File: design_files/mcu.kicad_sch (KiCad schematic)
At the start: 19 parts, among them J3 Conn_01x05, U1 STM32U545CEUx, U2 GD25QxxxEY, Y1 32.768KHz, Y2 8MHz

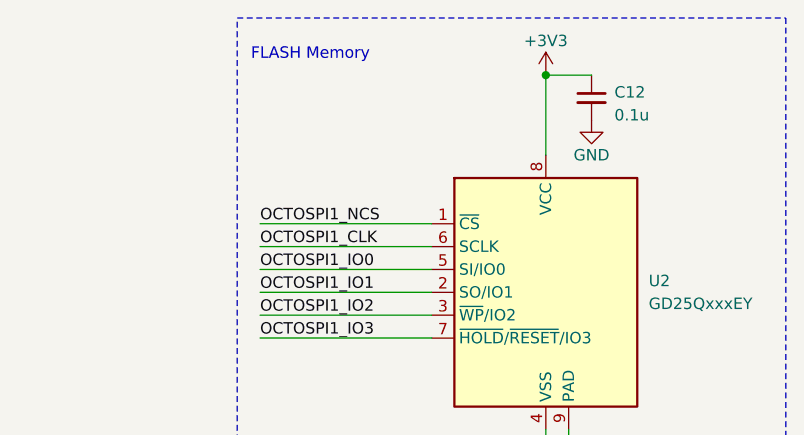
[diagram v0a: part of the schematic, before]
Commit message: Added CS pullup
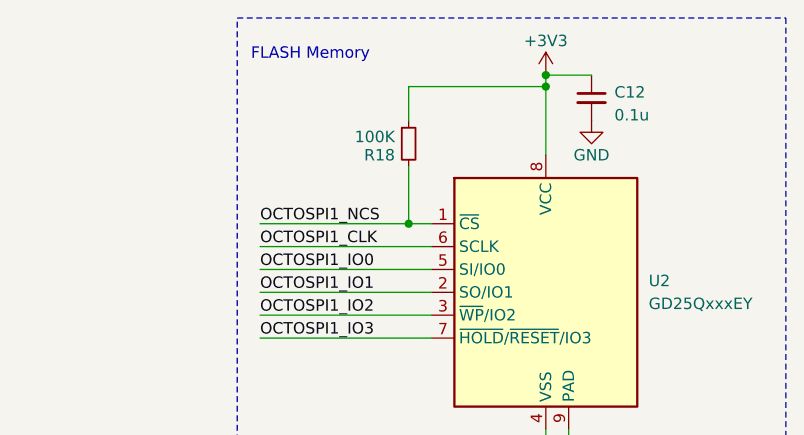
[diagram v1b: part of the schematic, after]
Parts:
- added R18: 100K, Resistor_SMD:R_0402_1005Metric, symbol Device:R_Small
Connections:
- net +3V3: now also R18.1
- net OCTOSPI1_NCS: now also R18.2
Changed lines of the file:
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@@
+	)
+	(junction
+		(at 252.73 22.86)
+		(diameter 0)
+		(color 0 0 0 0)
 	)
 	(junction
@@
 	)
 	(junction
+		(at 237.49 38.1)
+		(diameter 0)
+		(color 0 0 0 0)
+	)
+	(junction
 		(at 134.62 39.37)
 		(diameter 0)
@@
 	(wire
 		(pts
-			(xy 220.98 38.1) (xy 240.03 38.1)
+			(xy 220.98 38.1) (xy 237.49 38.1)
 		)
 		(stroke
@@
 	(wire
 		(pts
+			(xy 237.49 31.75) (xy 237.49 38.1)
+		)
+		(stroke
+			(width 0)
+			(type default)
+		)
+	)
+	(wire
+		(pts
 			(xy 152.4 62.23) (xy 152.4 67.31)
 		)
@@
 	(wire
 		(pts
+			(xy 252.73 22.86) (xy 252.73 30.48)
+		)
+		(stroke
+			(width 0)
+			(type default)
+		)
+	)
+	(wire
+		(pts
 			(xy 113.03 74.93) (xy 137.16 74.93)
 		)
@@
 	(wire
 		(pts
+			(xy 237.49 26.67) (xy 237.49 22.86)
+		)
+		(stroke
+			(width 0)
+			(type default)
+		)
+	)
+	(wire
+		(pts
 			(xy 113.03 80.01) (xy 137.16 80.01)
 		)
@@
 	(wire
 		(pts
-			(xy 252.73 21.59) (xy 252.73 30.48)
+			(xy 252.73 21.59) (xy 252.73 22.86)
 		)
 		(stroke
@@
 	(wire
 		(pts
+			(xy 237.49 22.86) (xy 252.73 22.86)
+		)
+		(stroke
+			(width 0)
+			(type default)
+		)
+	)
+	(wire
+		(pts
 			(xy 187.96 38.1) (xy 187.96 39.37)
 		)
@@
 		(pts
 			(xy 157.48 39.37) (xy 157.48 67.31)
+		)
+		(stroke
+			(width 0)
+			(type default)
+		)
+	)
+	(wire
+		(pts
+			(xy 237.49 38.1) (xy 240.03 38.1)
 		)
 		(stroke
@@
 					(unit 1)
 				)
+			)
+		)
+	)
+	(symbol
+		(lib_id "Device:R_Small")
+		(at 237.49 29.21 0)
+		(unit 1)
+		(exclude_from_sim no)
+		(in_bom yes)
+		(on_board yes)
+		(dnp no)
+		(property "Reference" "R18"
+			(at 235.966 30.48 0)
+			(effects
+				(font
+					(size 1.27 1.27)
+				)
+				(justify right)
+			)
+		)
+		(property "Value" "100K"
+			(at 235.966 28.448 0)
+			(effects
+				(font
+					(size 1.27 1.27)
+				)
+				(justify right)
+			)
+		)
+		(property "Footprint" "Resistor_SMD:R_0402_1005Metric"
+			(at 237.49 29.21 0)
+			(effects
+				(font
+					(size 1.27 1.27)
+				)
+				(hide yes)
+			)
+		)
+		(property "Datasheet" "~"
+			(at 237.49 29.21 0)
+			(effects
+				(font
+					(size 1.27 1.27)
+				)
+				(hide yes)
+			)
+		)
+		(property "Description" "Resistor, small symbol"
+			(at 237.49 29.21 0)
+			(effects
+				(font
+					(size 1.27 1.27)
+				)
+				(hide yes)
+			)
+		)
+		(pin "1"
+		)
+		(pin "2"
+		)
+		(instances
+			(project "tracker"
+				(path "/4f1d18f5-7d2b-4d0b-8633-b1619d53124c/5edf3f23-50ab-4fd8-9879-f628dc9bcaf7"
+					(reference "R18")
+					(unit 1)
+				)

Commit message: First review.
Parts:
- added R20: 10K, Resistor_SMD:R_0402_1005Metric, symbol Device:R_Small
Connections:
- net +3V3: now also R20.1
- net GSM_STATUS: now also R20.2
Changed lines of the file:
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@@
 	)
 	(junction
+		(at 107.95 85.09)
+		(diameter 0)
+		(color 0 0 0 0)
+	)
+	(junction
 		(at 134.62 39.37)
 		(diameter 0)
@@
 	(wire
 		(pts
+			(xy 107.95 81.28) (xy 107.95 85.09)
+		)
+		(stroke
+			(width 0)
+			(type default)
+		)
+	)
+	(wire
+		(pts
 			(xy 167.64 102.87) (xy 205.74 102.87)
 		)
@@
 	(wire
 		(pts
+			(xy 107.95 74.93) (xy 107.95 76.2)
+		)
+		(stroke
+			(width 0)
+			(type default)
+		)
+	)
+	(wire
+		(pts
 			(xy 48.26 152.4) (xy 48.26 154.94)
 		)
@@
 	(wire
 		(pts
-			(xy 102.87 85.09) (xy 137.16 85.09)
+			(xy 102.87 85.09) (xy 107.95 85.09)
 		)
 		(stroke
@@
 	(wire
 		(pts
+			(xy 107.95 85.09) (xy 137.16 85.09)
+		)
+		(stroke
+			(width 0)
+			(type default)
+		)
+	)
+	(wire
+		(pts
 			(xy 104.14 118.11) (xy 137.16 118.11)
 		)
@@
 	)
 	(symbol
+		(lib_id "Device:R_Small")
+		(at 107.95 78.74 0)
+		(mirror y)
+		(unit 1)
+		(exclude_from_sim no)
+		(in_bom yes)
+		(on_board yes)
+		(dnp no)
+		(property "Reference" "R20"
+			(at 102.616 79.756 0)
+			(effects
+				(font
+					(size 1.27 1.27)
+				)
+				(justify right)
+			)
+		)
+		(property "Value" "10K"
+			(at 102.362 77.724 0)
+			(effects
+				(font
+					(size 1.27 1.27)
+				)
+				(justify right)
+			)
+		)
+		(property "Footprint" "Resistor_SMD:R_0402_1005Metric"
+			(at 107.95 78.74 0)
+			(effects
+				(font
+					(size 1.27 1.27)
+				)
+				(hide yes)
+			)
+		)
+		(property "Datasheet" "~"
+			(at 107.95 78.74 0)
+			(effects
+				(font
+					(size 1.27 1.27)
+				)
+				(hide yes)
+			)
+		)
+		(property "Description" "Resistor, small symbol"
+			(at 107.95 78.74 0)
+			(effects
+				(font
+					(size 1.27 1.27)
+				)
+				(hide yes)
+			)
+		)
+		(pin "1"
+		)
+		(pin "2"
+		)
+		(instances
+			(project "tracker"
+				(path "/4f1d18f5-7d2b-4d0b-8633-b1619d53124c/5edf3f23-50ab-4fd8-9879-f628dc9bcaf7"
+					(reference "R20")
+					(unit 1)
+				)
+			)
+		)
+	)
+	(symbol
 		(lib_id "power:+3.3V")
 		(at 252.73 21.59 0)
@@
 					(unit 1)
 				)
+			)
+		)
+	)
+	(symbol
+		(lib_id "power:+3.3V")
+		(at 107.95 74.93 0)
+		(unit 1)
+		(exclude_from_sim no)
+		(in_bom yes)
+		(on_board yes)
+		(dnp no)
+		(fields_autoplaced yes)
+		(property "Reference" "#PWR043"
+			(at 107.95 78.74 0)
+			(effects
+				(font
+					(size 1.27 1.27)
+				)
+				(hide yes)
+			)
+		)
+		(property "Value" "+3V3"
+			(at 107.95 71.12 0)
+			(effects
+				(font
+					(size 1.27 1.27)
+				)
+			)
+		)
+		(property "Footprint" ""
+			(at 107.95 74.93 0)
+			(effects
+				(font
+					(size 1.27 1.27)
+				)
+				(hide yes)
+			)
+		)
+		(property "Datasheet" ""
+			(at 107.95 74.93 0)
+			(effects
+				(font
+					(size 1.27 1.27)
+				)
+				(hide yes)
+			)
+		)
+		(property "Description" "Power symbol creates a global label with name \"+3.3V\""
+			(at 107.95 74.93 0)
+			(effects
+				(font
+					(size 1.27 1.27)
+				)
+				(hide yes)
+			)
+		)
+		(pin "1"
+		)
+		(instances
+			(project "tracker"
+				(path "/4f1d18f5-7d2b-4d0b-8633-b1619d53124c/5edf3f23-50ab-4fd8-9879-f628dc9bcaf7"
+					(reference "#PWR043")
+					(unit 1)
+				)
